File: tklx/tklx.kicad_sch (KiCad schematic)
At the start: 226 parts, among them J1 USB_C_Receptacle_USB2.0_14P, J2 Conn_01x04, SW1 SW_Push, SW2 SW_Push, U1 ESP32-S2, U2 XC6206PxxxMR, U3 SRV05-4

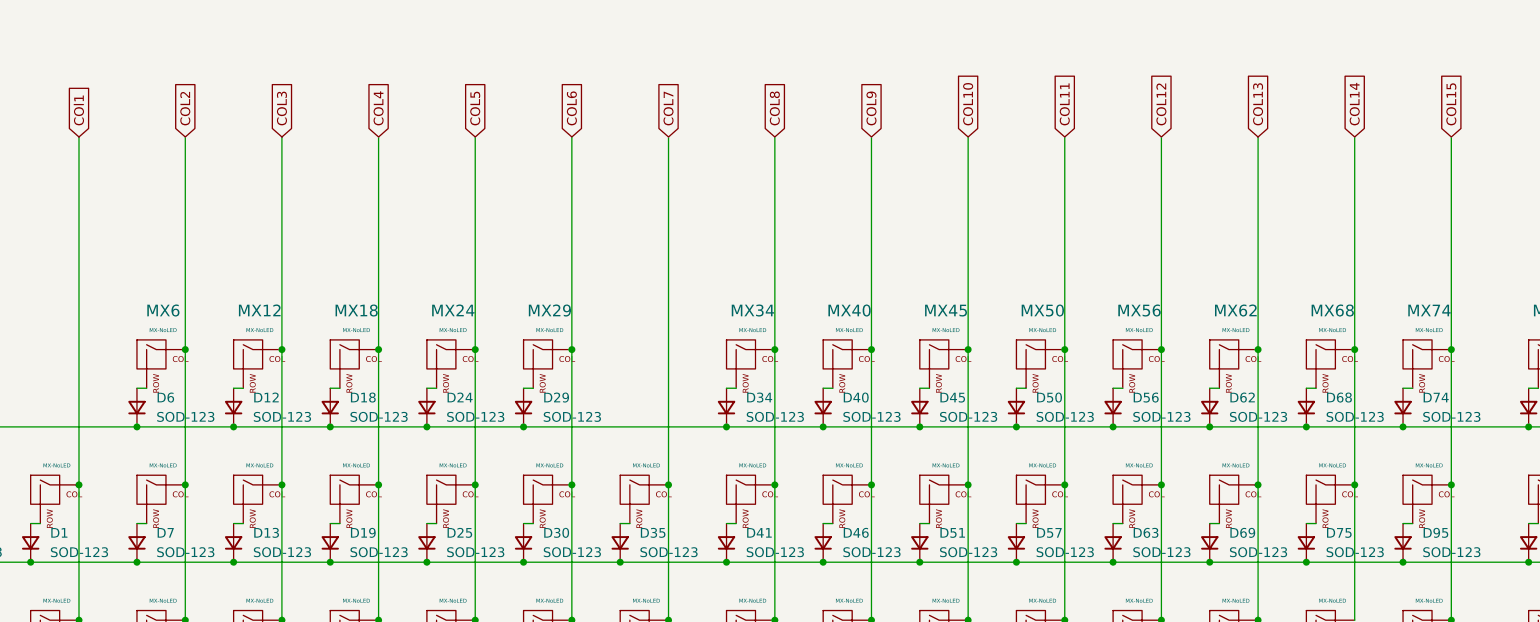
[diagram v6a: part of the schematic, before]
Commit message: added support for f13 row
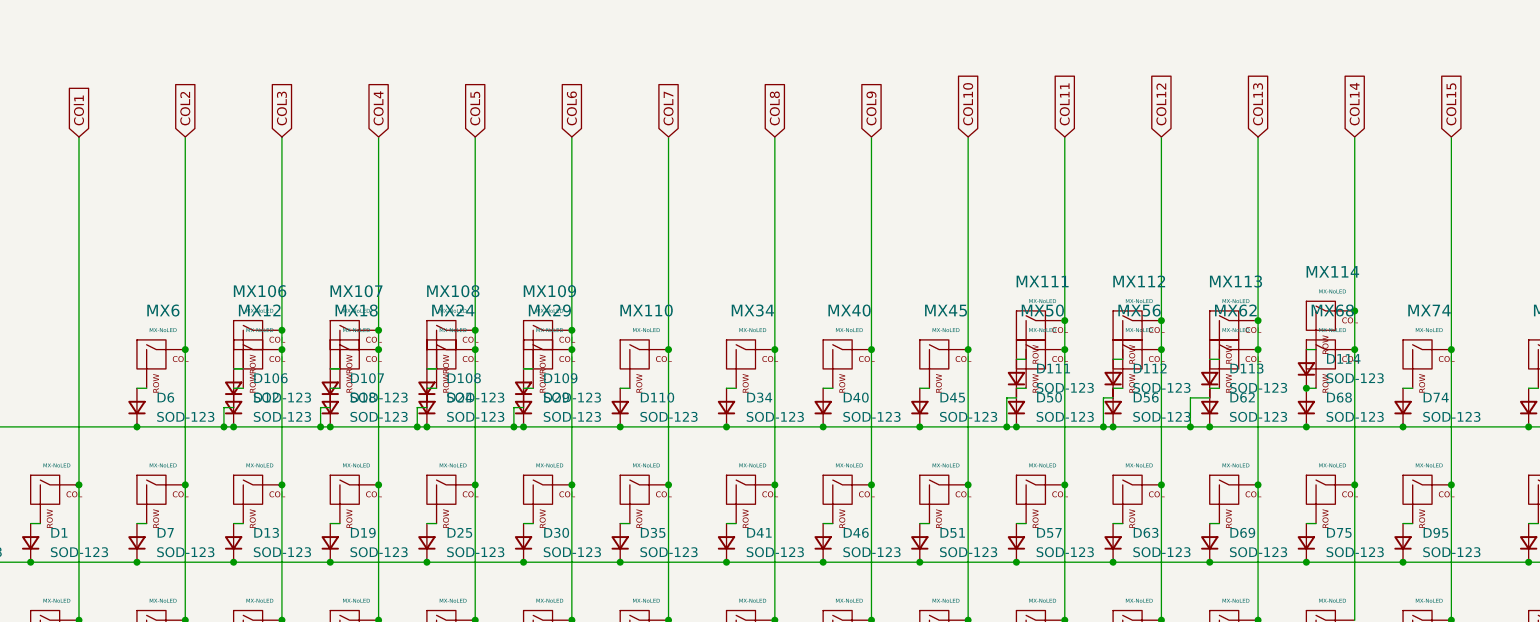
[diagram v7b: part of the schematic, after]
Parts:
- added D106, D107, D108, D109, D110, D111, D112, D113, D114: SOD-123, Diode_SMD:D_SOD-123, symbol Device:D_Small
- added MX106, MX107, MX108, MX109, MX110, MX111, MX112, MX113, MX114: MX-NoLED, MX_Only:MXOnly-1U-NoLED, symbol MX_Alps_Hybrid:MX-NoLED
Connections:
- net COL11: now also MX111.1 (COL)
- net COL12: now also MX112.1 (COL)
- net COL13: now also MX113.1 (COL)
- net COL14: now also MX114.1 (COL)
- net COL3: now also MX106.1 (COL)
- net COL4: now also MX107.1 (COL)
- net COL5: now also MX108.1 (COL)
- net COL6: now also MX109.1 (COL)
- net COL7: now also MX110.1 (COL)
- net ROW0: now also D106.1 (K), D107.1 (K), D108.1 (K), D109.1 (K), D110.1 (K), D111.1 (K), D112.1 (K), D113.1 (K)
- net at D68.2 (A), MX68.2 (ROW): now also D114.1 (K)
- new net: D109.2 (A), MX109.2 (ROW)
- new net: D113.2 (A), MX113.2 (ROW)
- new net: D110.2 (A), MX110.2 (ROW)
- new net: D107.2 (A), MX107.2 (ROW)
- new net: D114.2 (A), MX114.2 (ROW)
- new net: D112.2 (A), MX112.2 (ROW)
- new net: D106.2 (A), MX106.2 (ROW)
- new net: D108.2 (A), MX108.2 (ROW)
- new net: D111.2 (A), MX111.2 (ROW)

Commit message: intial stm32 design
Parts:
- removed J2: Conn_01x04, Connector_JST:JST_SH_SM04B-SRSS-TB_1x04-1MP_P1.00mm_Horizontal, symbol Connector_Generic:Conn_01x04
- removed R7: 1K, Resistor_SMD:R_0402_1005Metric, symbol Device:R_Small
- removed R8, R9: 5.1k, Resistor_SMD:R_0402_1005Metric, symbol Device:R_Small
- removed SW2: SW_Push, Button_Switch_SMD:SW_Push_SPST_NO_Alps_SKRK, symbol Switch:SW_Push
- removed U1: ESP32-S2, Package_DFN_QFN:QFN-56-1EP_7x7mm_P0.4mm_EP5.6x5.6mm, symbol PCM_Espressif:ESP32-S2
- added U1: TLV75801PDRV, Package_SON:WSON-6-1EP_2x2mm_P0.65mm_EP1x1.6mm, symbol Regulator_Linear:TLV75801PDRV
- added U4: ESP32-S3, Package_DFN_QFN:QFN-56-1EP_7x7mm_P0.4mm_EP5.6x5.6mm, symbol PCM_Espressif:ESP32-S3
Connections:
- net COL0: now also U4.6 (GPIO1/ADC1_CH0)
- net COL10: now also U4.16 (GPIO11/ADC2_CH0)
- net COL11: now also U4.17 (GPIO12/ADC2_CH1)
- net COL12: now also U4.18 (GPIO13/ADC2_CH2)
- net COL13: now also U4.19 (GPIO14/ADC2_CH3)
- net COL14: now also U4.23 (GPIO17/ADC2_CH6)
- net COL15: now also U4.24 (GPIO18/ADC2_CH7)
- net COL16: now also U4.27 (GPIO21)
- net COL17: now also U4.43 (GPIO38)
- net COL18: now also U4.51 (GPIO45)
- net COL2: now also U4.8 (GPIO3/ADC1_CH2); no longer MX72.1 (COL)
- net COL3: now also U4.9 (GPIO4/ADC1_CH3)
- net COL4: now also U4.10 (GPIO5/ADC1_CH4)
- net COL5: now also U4.11 (GPIO6/ADC1_CH5)
- net COL6: now also U4.12 (GPIO7/ADC1_CH6)
- net COL7: now also U4.13 (GPIO8/ADC1_CH7)
- net COL8: now also U4.14 (GPIO9/ADC1_CH8)
- net COL9: now also U4.15 (GPIO10/ADC1_CH9)
- net D+: now also U4.26 (GPIO20/USB_D+/ADC2_CH9)
- net D-: now also U4.25 (GPIO19/USB_D-/ADC2_CH8)
- net GND: now also U4.57 (GND)
- net RESET: now also U4.4 (CHIP_PU/RESET)
- net ROW0: now also D114.1 (K), U4.52 (GPIO46)
- net ROW1: now also U4.42 (GPIO37)
- net ROW2: now also U4.41 (GPIO36)
- net ROW3: now also U4.40 (GPIO35)
- net ROW4: now also U4.39 (GPIO34)
- net ROW5: now also U4.38 (GPIO33)
- net at D68.2 (A), MX68.2 (ROW): no longer D114.1 (K)
- new net: U1.3 (GND), U1.7 (GND)
- new net: U4.55 (VDDA), U4.56 (VDDA)
- new net BOOT: U4.5 (GPIO0/BOOT)
- new net COL1: U4.7 (GPIO2/ADC1_CH1)
- new net VDD3P3: U4.2 (VDD3P3), U4.3 (VDD3P3)
- no-connect marks 2 -> 6
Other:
- moved on the sheet: D101, D106, D107, D108, D109, D111, D112, D113, D114, D72, D78, D89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
